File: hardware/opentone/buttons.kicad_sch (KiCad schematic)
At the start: 9 parts

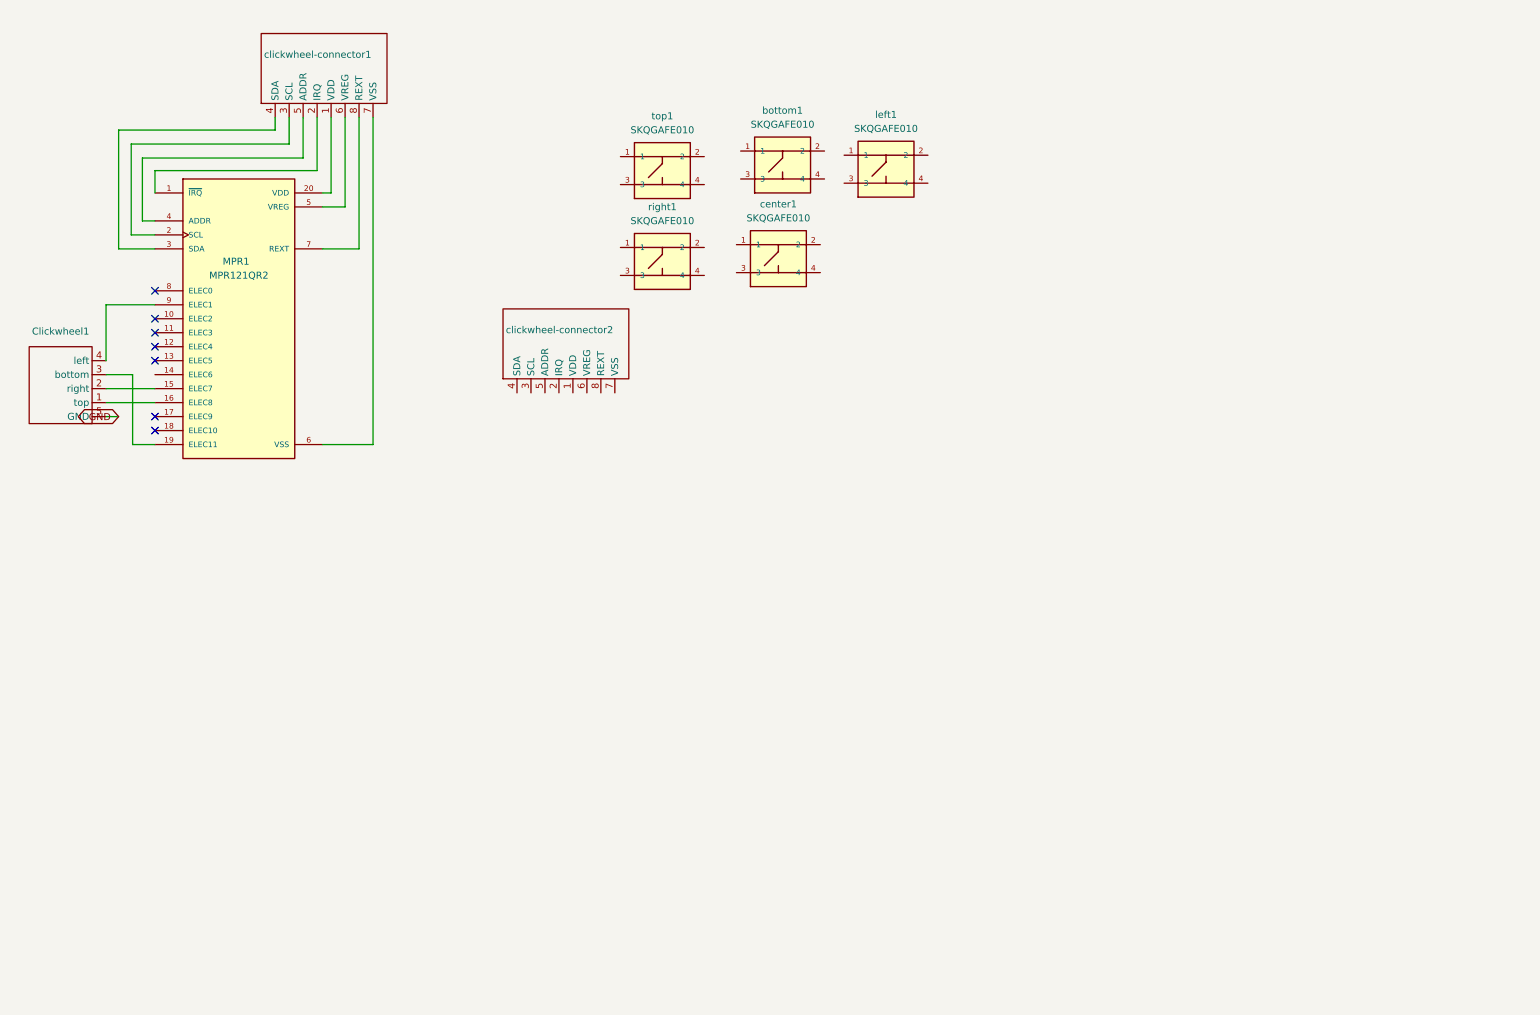
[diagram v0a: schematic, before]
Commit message: updated buttons and MCU
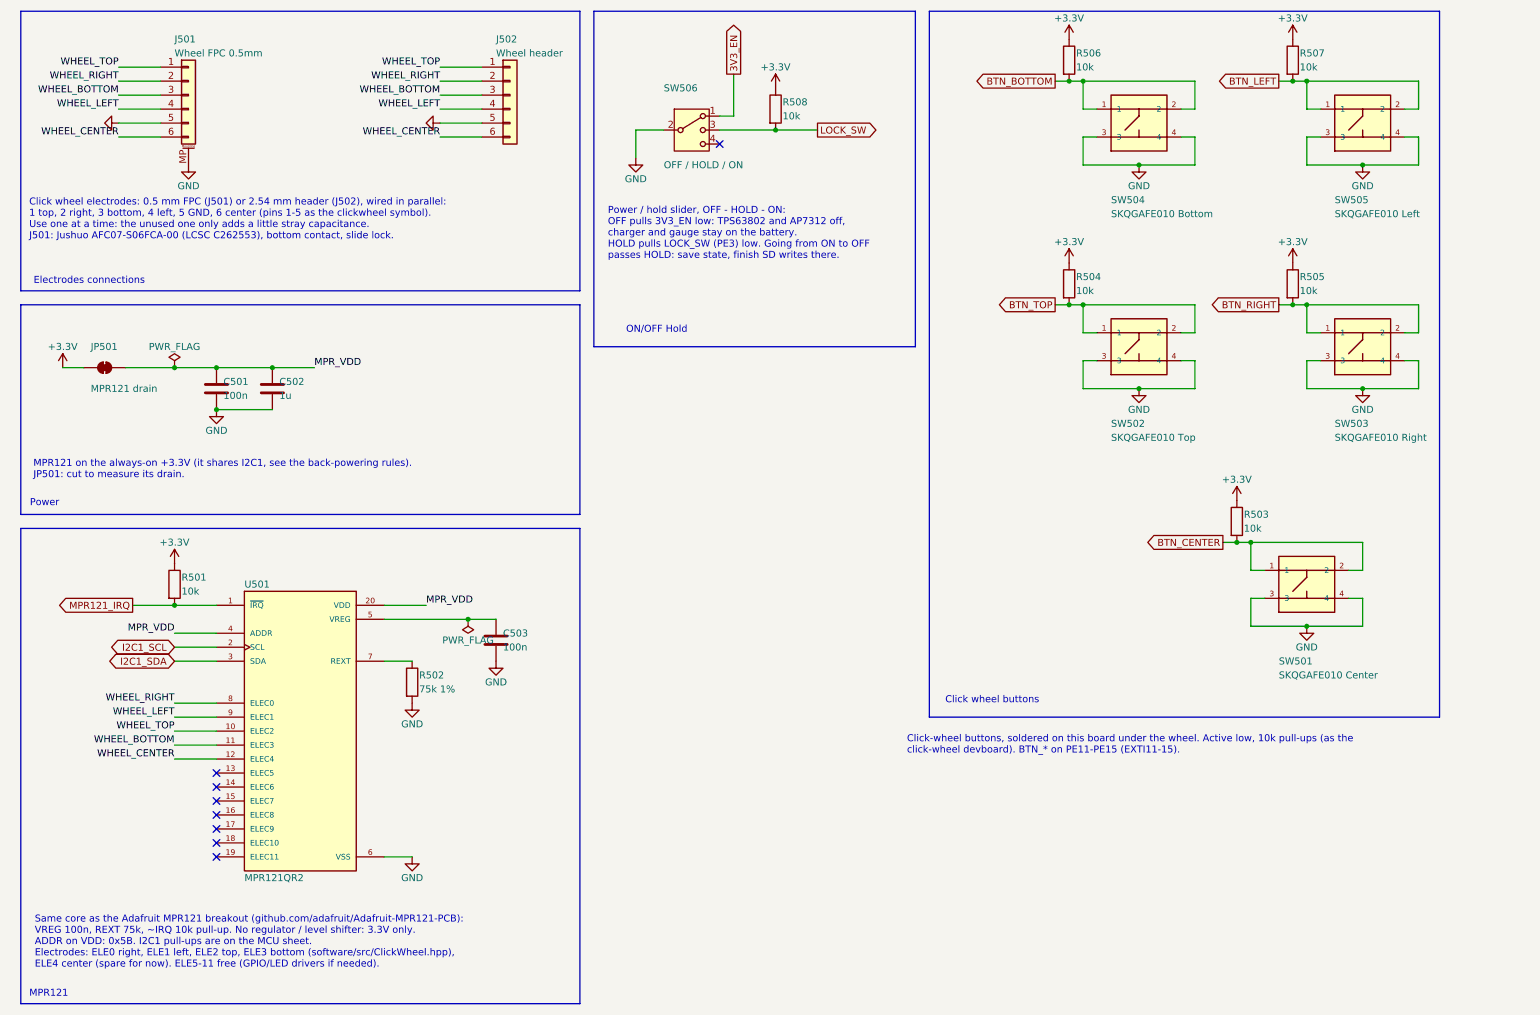
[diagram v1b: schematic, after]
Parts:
- removed Clickwheel1: ~, opentone:clickwheel_1, symbol opentone:clickwheel
- removed MPR1: MPR121QR2, opentone:mpr121qr2, symbol opentone:MPR121QR2
- removed bottom1, center1, left1, right1, top1: SKQGAFE010, opentone:SW_SKQGAFE010, symbol opentone:SKQGAFE010
- removed clickwheel-connector1, clickwheel-connector2: ~, Connector_FFC-FPC:Hirose_FH12-8S-0.5SH_1x08-1MP_P0.50mm_Horizontal, symbol opentone:clickwheel-connector
- added C501, C503: 100n, Capacitor_SMD:C_0805_2012Metric, symbol Device:C
- added C502: 1u, Capacitor_SMD:C_0805_2012Metric, symbol Device:C
- added J501: Wheel FPC 0.5mm, Connector_FFC-FPC:Jushuo_AFC07-S06FCA-00_1x6-1MP_P0.50_Horizontal, symbol Connector_Generic_MountingPin:Conn_01x06_MountingPin
- added J502: Wheel header, Connector_PinHeader_2.54mm:PinHeader_1x06_P2.54mm_Vertical, symbol Connector_Generic:Conn_01x06
- added JP501: MPR121 drain, Jumper:SolderJumper-2_P1.3mm_Bridged_RoundedPad1.0x1.5mm, symbol Jumper:SolderJumper_2_Bridged
- added R501, R503, R504, R505, R506, R507, R508: 10k, Resistor_SMD:R_0805_2012Metric, symbol Device:R
- added R502: 75k 1%, Resistor_SMD:R_0805_2012Metric, symbol Device:R
- added SW501: SKQGAFE010 Center, opentone:SW_SKQGAFE010, symbol opentone:SKQGAFE010
- added SW502: SKQGAFE010 Top, opentone:SW_SKQGAFE010, symbol opentone:SKQGAFE010
- added SW503: SKQGAFE010 Right, opentone:SW_SKQGAFE010, symbol opentone:SKQGAFE010
- added SW504: SKQGAFE010 Bottom, opentone:SW_SKQGAFE010, symbol opentone:SKQGAFE010
- added SW505: SKQGAFE010 Left, opentone:SW_SKQGAFE010, symbol opentone:SKQGAFE010
- added SW506: OFF / HOLD / ON, Button_Switch_THT:SW_Slide_SP3T_Straight_CK_OS103012MU1QP1, symbol opentone:SW_SP3T_OS103
- added U501: MPR121QR2, opentone:mpr121qr2, symbol opentone:MPR121QR2
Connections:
- net GND: now also C501.2, C502.2, C503.2, J501.5 (Pin_5), J501.MP (MountPin), J502.5 (Pin_5), R502.2, SW501.3, SW501.4, SW502.3, SW502.4, SW503.3, SW503.4, SW504.3, SW504.4, SW505.3, SW505.4, SW506.2, U501.6 (VSS)
- new net: R502.1, U501.7 (REXT)
- new net: C503.1, U501.5 (VREG)
- new net +3.3V: JP501.1 (A), R501.1, R503.1, R504.1, R505.1, R506.1, R507.1, R508.1
- new net 3V3_EN: SW506.1
- new net BTN_BOTTOM: R506.2, SW504.1, SW504.2
- new net BTN_CENTER: R503.2, SW501.1, SW501.2
- new net BTN_LEFT: R507.2, SW505.1, SW505.2
- new net BTN_RIGHT: R505.2, SW503.1, SW503.2
- new net BTN_TOP: R504.2, SW502.1, SW502.2
- new net I2C1_SCL: U501.2 (SCL)
- new net I2C1_SDA: U501.3 (SDA)
- new net LOCK_SW: R508.2, SW506.3
- new net MPR121_IRQ: R501.2, U501.1 (~{IRQ})
- new net MPR_VDD: C501.1, C502.1, JP501.2 (B), U501.20 (VDD), U501.4 (ADDR)
- new net WHEEL_BOTTOM: J501.3 (Pin_3), J502.3 (Pin_3), U501.11 (ELEC3)
- new net WHEEL_CENTER: J501.6 (Pin_6), J502.6 (Pin_6), U501.12 (ELEC4)
- new net WHEEL_LEFT: J501.4 (Pin_4), J502.4 (Pin_4), U501.9 (ELEC1)
- new net WHEEL_RIGHT: J501.2 (Pin_2), J502.2 (Pin_2), U501.8 (ELEC0)
- new net WHEEL_TOP: J501.1 (Pin_1), J502.1 (Pin_1), U501.10 (ELEC2)
- no-connect marks 7 -> 8
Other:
- note added: "Click wheel buttons"
- note added: "Click wheel electrodes: 0.5 mm FPC (J501) or 2.54 mm header (J502), wired in parallel: 1 top, 2 right, 3 bottom, 4 left, 5 GND, 6 center (pins 1-5 as the clickwheel symbol). Use one at a time: the unused one only adds a little stray capacitance. J501: Jushuo AFC07-S06FCA-00 (LCSC C262553), bottom contact, slide lock."
- note added: "Click-wheel buttons, soldered on this board under the wheel. Active low, 10k pull-ups (as the click-wheel devboard). BTN_* on PE11-PE15 (EXTI11-15)."
- note added: "Electrodes connections"
- note added: "MPR121"
- note added: "MPR121 on the always-on +3.3V (it shares I2C1, see the back-powering rules). JP501: cut to measure its drain."
- note added: "ON/OFF Hold"
- note added: "Power"
- note added: "Power / hold slider, OFF - HOLD - ON: OFF pulls 3V3_EN low: TPS63802 and AP7312 off, charger and gauge stay on the battery. HOLD pulls LOCK_SW (PE3) low. Going from ON to OFF passes HOLD: save state, finish SD writes there."
- note added: "Same core as the Adafruit MPR121 breakout (github.com/adafruit/Adafruit-MPR121-PCB): VREG 100n, REXT 75k, ~IRQ 10k pull-up. No regulator / level shifter: 3.3V only. ADDR on VDD: 0x5B. I2C1 pull-ups are on the MCU sheet. Electrodes: ELE0 right, ELE1 left, ELE2 top, ELE3 bottom (software/src/ClickWheel.hpp), ELE4 center (spare for now). ELE5-11 free (GPIO/LED drivers if needed)."
- title: (none) -> Buttons

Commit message: added sd card, haptic, updated old parts and set a datasheet and MPN to all parts
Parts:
- added C504, C506: 1u, Capacitor_SMD:C_0603_1608Metric, symbol Device:C
- added C505: 100n, Capacitor_SMD:C_0603_1608Metric, symbol Device:C
- added JP502: Haptic drain, Jumper:SolderJumper-2_P1.3mm_Bridged_RoundedPad1.0x1.5mm, symbol Jumper:SolderJumper_2_Bridged
- added R509: 100k, Resistor_SMD:R_0603_1608Metric, symbol Device:R
- added TP501: M+, TestPoint:TestPoint_Pad_1.5x1.5mm, symbol Connector:TestPoint
- added TP502: M-, TestPoint:TestPoint_Pad_1.5x1.5mm, symbol Connector:TestPoint
- added U502: DRV2605L, Package_SO:VSSOP-10_3x3mm_P0.5mm, symbol Driver_Haptic:DRV2605LDGS
- C501, C503: footprint Capacitor_SMD:C_0805_2012Metric -> Capacitor_SMD:C_0603_1608Metric; LCSC (none) -> C14663; Manufacturer (none) -> YAGEO; Part number (none) -> CC0603KRX7R9BB104
- C502: footprint Capacitor_SMD:C_0805_2012Metric -> Capacitor_SMD:C_0603_1608Metric; LCSC (none) -> C15849; Manufacturer (none) -> Samsung Electro-Mechanics; Part number (none) -> CL10A105KB8NNNC
- J501, J502, JP501: now left out of the parts list
- R501, R503, R504, R505, R506, R507, R508: footprint Resistor_SMD:R_0805_2012Metric -> Resistor_SMD:R_0603_1608Metric; LCSC (none) -> C25804; Manufacturer (none) -> UNI-ROYAL; Part number (none) -> 0603WAF1002T5E
- R502: footprint Resistor_SMD:R_0805_2012Metric -> Resistor_SMD:R_0603_1608Metric; LCSC (none) -> C23242; Manufacturer (none) -> UNI-ROYAL; Part number (none) -> 0603WAF7502T5E
- SW501, SW502, SW503, SW504, SW505: LCSC (none) -> C202424
- SW506: footprint Button_Switch_THT:SW_Slide_SP3T_Straight_CK_OS103012MU1QP1 -> Button_Switch_SMD:SW_SP3T_PCM13; symbol opentone:SW_SP3T_OS103 -> opentone:SW_SP3T_PCM13; LCSC C221831 -> (none); Part number OS103011MS8QP1 -> PCM13SMTR
- U501: LCSC (none) -> C91322
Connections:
- net +3.3V: now also JP502.1 (A)
- net GND: now also SW506.3, C504.2, C505.2, C506.2, R509.2, U502.4 (IN/TRIG), U502.8 (GND); no longer SW506.2
- net I2C1_SCL: now also U502.2 (SCL)
- net I2C1_SDA: now also U502.3 (SDA)
- net LOCK_SW: now also SW506.2; no longer SW506.3
- new net: C506.1, U502.1 (REG)
- new net: TP501.1, U502.7 (OUT+)
- new net: TP502.1, U502.9 (OUT-)
- new net DRV_EN: R509.1, U502.5 (EN)
- new net DRV_VDD: C504.1, C505.1, JP502.2 (B), U502.10 (VDD), U502.6 (VDD/NC)
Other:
- note added: "Haptics: DRV2605L, 10 mm coin ERM on M+/M- pads. +3.3V -> JP502 (cut to measure) -> DRV_VDD. I2C1 at 0x5A. EN = DRV_EN (PB5), R509 pull-down: shutdown while the MCU is off. IN/TRIG to GND (internal trigger)."
- note added: "Power / hold slider, OFF - HOLD - ON: OFF pulls 3V3_EN low: TPS63802 off (so the MCU, and with it VS_EN: VS1053 LDOs off too). DRV2605L off too. Charger and gauge stay on the battery. HOLD pulls LOCK_SW (PE3) low. Going from ON to OFF passes HOLD: save state, finish SD writes there."
- note removed: "Power / hold slider, OFF - HOLD - ON: OFF pulls 3V3_EN low: TPS63802 and AP7312 off, charger and gauge stay on the battery. HOLD pulls LOCK_SW (PE3) low. Going from ON to OFF passes HOLD: save state, finish SD writes there."

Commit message: updated BOM
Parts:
- C501, C503, C505: value 100n -> 100nF
- C502, C504, C506: value 1u -> 1uF
- R502: value 75k 1% -> 75k
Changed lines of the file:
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@@
 			)
 		)
-		(property "Value" "1u"
+		(property "Value" "1uF"
 			(at 172.72 92.71 0)
 			(show_name no)
@@
 			)
 		)
-		(property "Value" "1u"
+		(property "Value" "1uF"
 			(at 73.66 83.82 0)
 			(show_name no)
@@
 			)
 		)
-		(property "Value" "75k 1%"
+		(property "Value" "75k"
 			(at 99.06 137.16 0)
 			(show_name no)
@@
 			)
 		)
-		(property "Value" "1u"
+		(property "Value" "1uF"
 			(at 182.88 144.78 0)
 			(show_name no)
@@
 			)
 		)
-		(property "Value" "100n"
+		(property "Value" "100nF"
 			(at 182.88 92.71 0)
 			(show_name no)
@@
 			)
 		)
-		(property "Value" "100n"
+		(property "Value" "100nF"
 			(at 63.5 83.82 0)
 			(show_name no)
@@
 			)
 		)
-		(property "Value" "100n"
+		(property "Value" "100nF"
 			(at 114.3 129.54 0)
 			(show_name no)

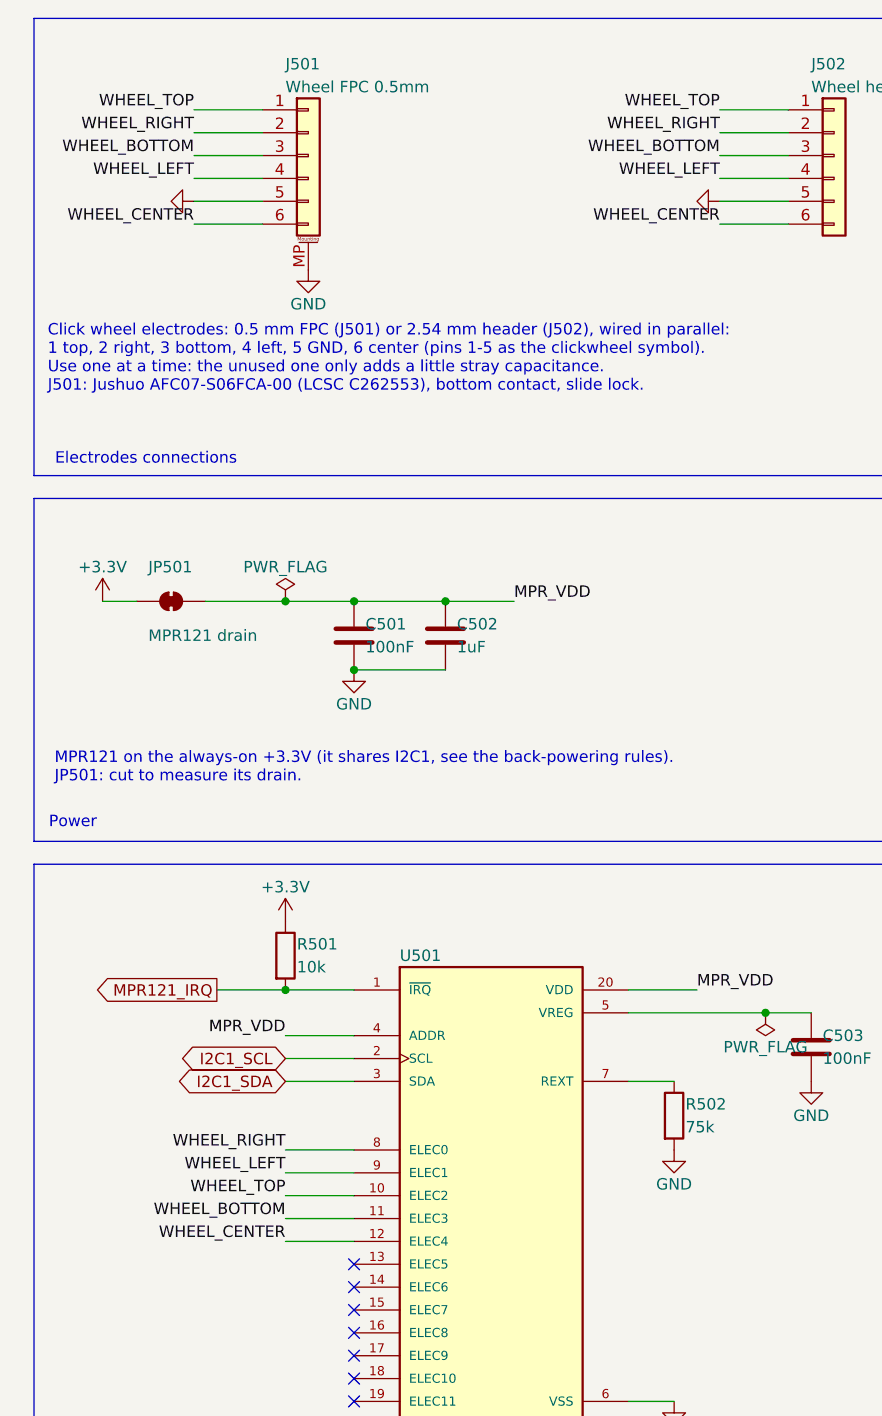
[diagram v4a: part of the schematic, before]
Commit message: started placing the components
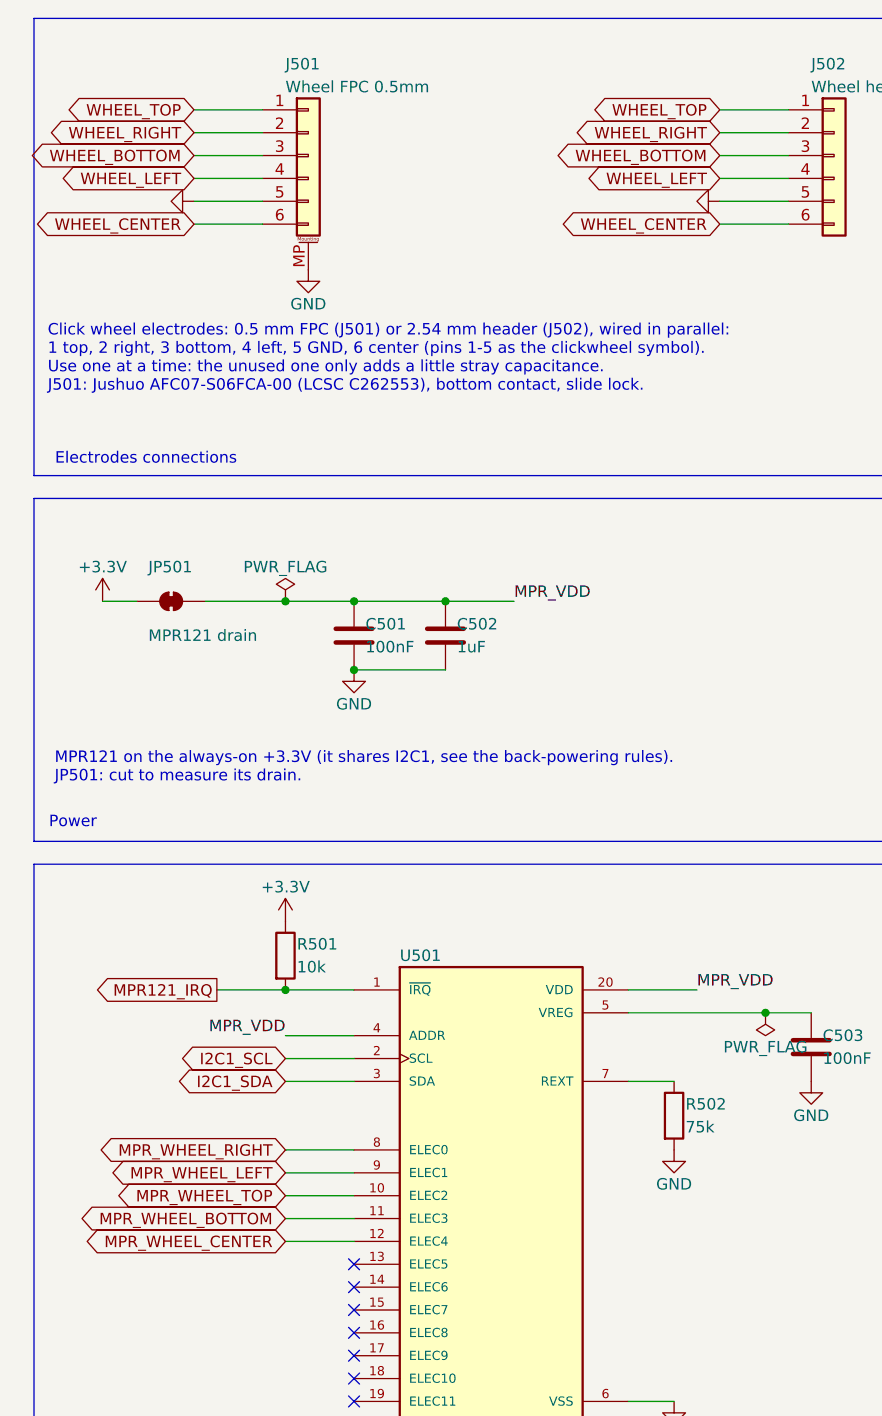
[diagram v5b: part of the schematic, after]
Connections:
- net WHEEL_BOTTOM: no longer U501.11 (ELEC3)
- net WHEEL_CENTER: no longer U501.12 (ELEC4)
- net WHEEL_LEFT: no longer U501.9 (ELEC1)
- net WHEEL_RIGHT: no longer U501.8 (ELEC0)
- net WHEEL_TOP: no longer U501.10 (ELEC2)
- new net MPR_WHEEL_BOTTOM: U501.11 (ELEC3)
- new net MPR_WHEEL_CENTER: U501.12 (ELEC4)
- new net MPR_WHEEL_LEFT: U501.9 (ELEC1)
- new net MPR_WHEEL_RIGHT: U501.8 (ELEC0)
- new net MPR_WHEEL_TOP: U501.10 (ELEC2)
